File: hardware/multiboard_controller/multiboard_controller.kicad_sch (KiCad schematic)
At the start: 0 parts

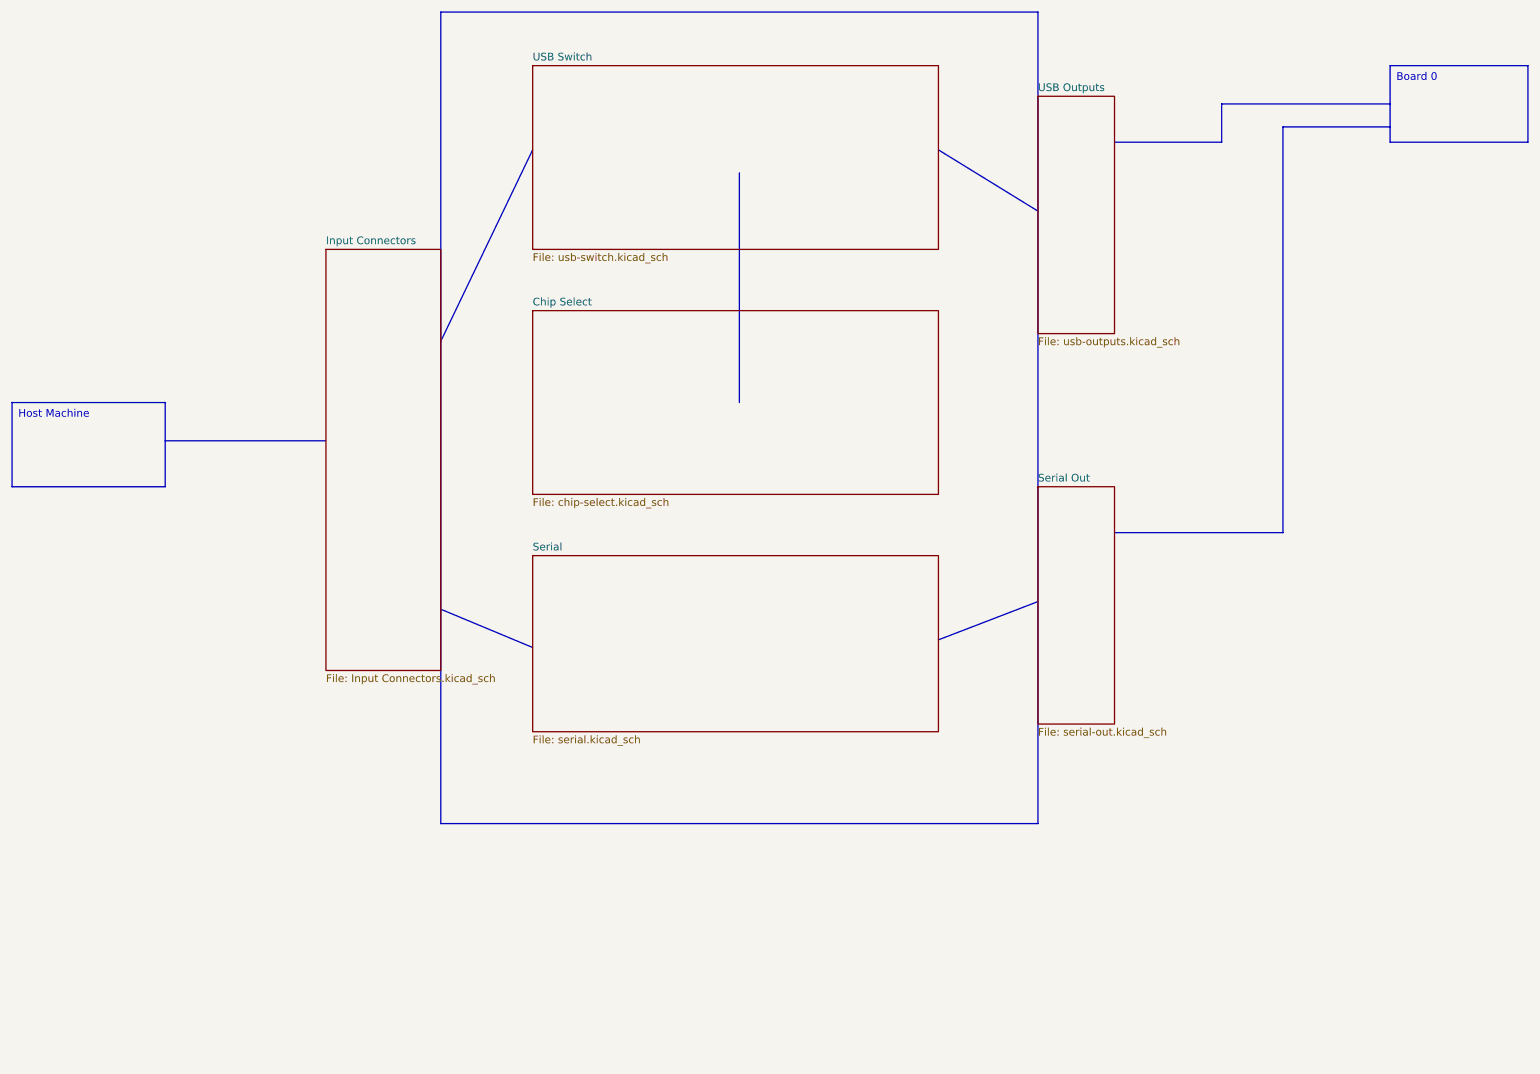
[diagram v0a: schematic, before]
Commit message: Add ESD protection for USB 2.0 ifaces.
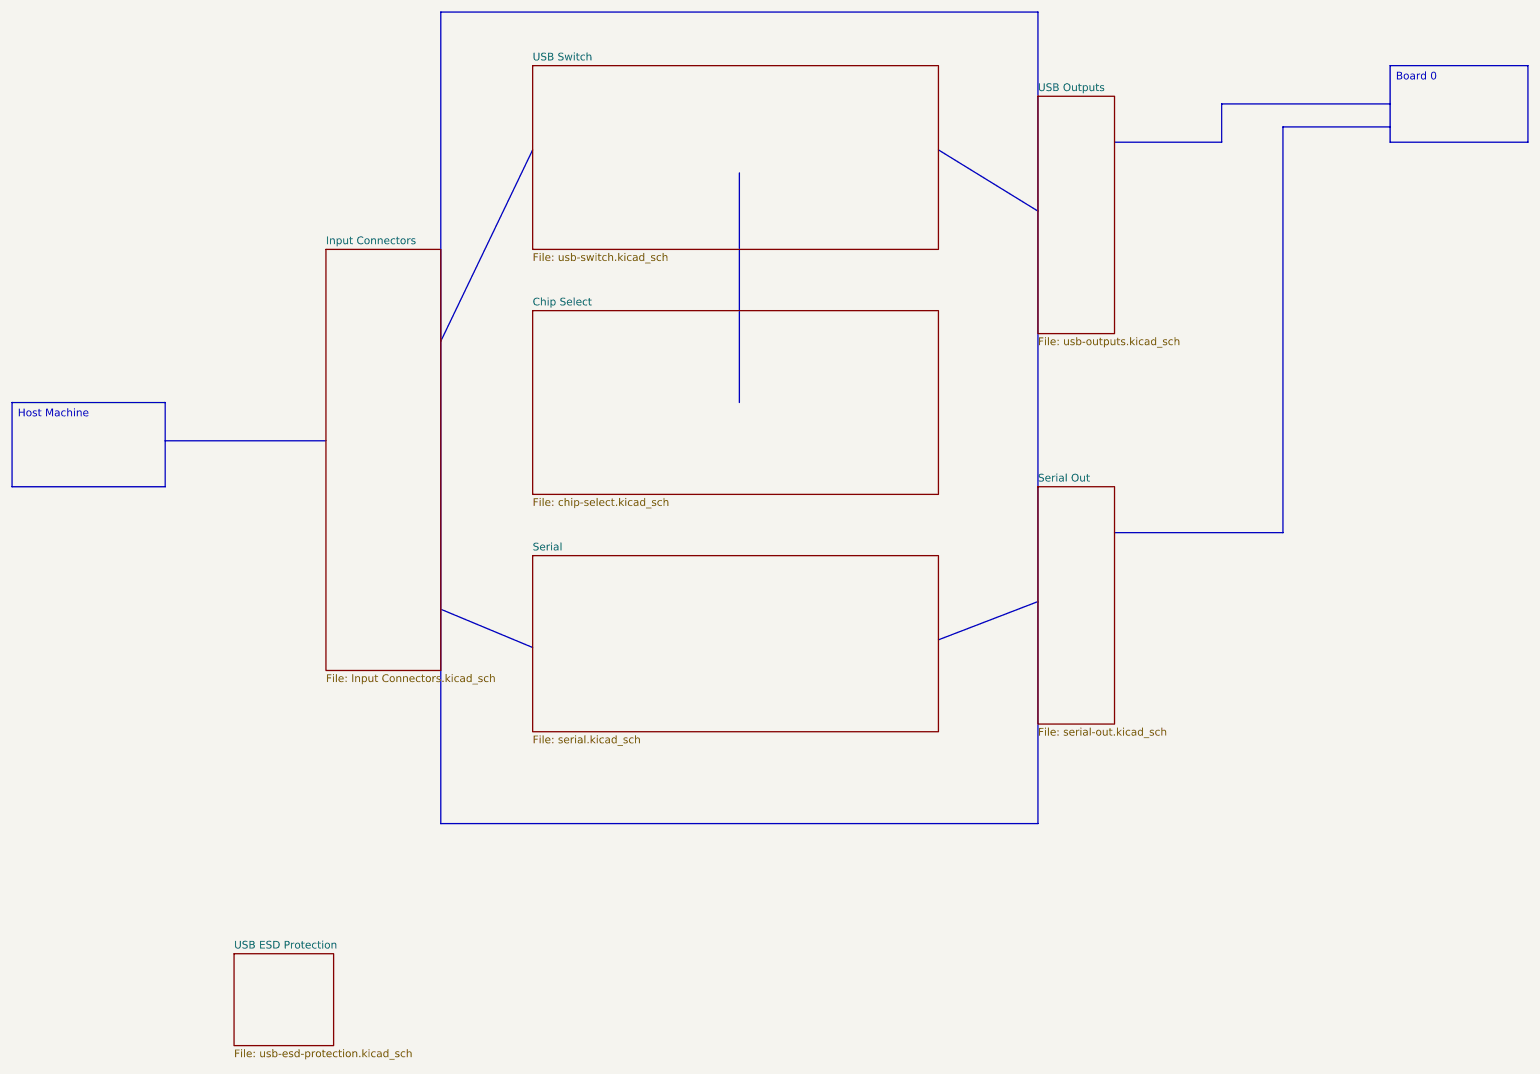
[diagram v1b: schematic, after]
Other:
- added sheet USB ESD Protection (usb-esd-protection.kicad_sch)
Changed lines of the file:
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@@
 (kicad_sch
-	(version 20231120)
+	(version 20250114)
 	(generator "eeschema")
-	(generator_version "8.0")
+	(generator_version "9.0")
 	(paper "A4")
 	(title_block
@@
 		(date "2025-02-12")
 	)
-	(polyline
-		(pts
-			(xy 90.17 72.39) (xy 105.41 40.64)
-		)
-		(stroke
-			(width 0)
-			(type default)
-		)
-	)
-	(polyline
-		(pts
-			(xy 90.17 116.84) (xy 105.41 123.19)
-		)
-		(stroke
-			(width 0)
-			(type default)
-		)
-	)
-	(polyline
-		(pts
-			(xy 219.71 39.37) (xy 219.71 33.02)
-		)
-		(stroke
-			(width 0)
-			(type default)
-		)
-	)
-	(polyline
-		(pts
-			(xy 44.45 88.9) (xy 71.12 88.9)
-		)
-		(stroke
-			(width 0)
-			(type default)
-		)
-	)
-	(polyline
-		(pts
-			(xy 172.72 121.92) (xy 189.23 115.57)
-		)
-		(stroke
-			(width 0)
-			(type default)
-		)
-	)
-	(polyline
-		(pts
-			(xy 229.87 36.83) (xy 247.65 36.83)
-		)
-		(stroke
-			(width 0)
-			(type default)
-		)
-	)
-	(polyline
-		(pts
-			(xy 172.72 40.64) (xy 189.23 50.8)
-		)
-		(stroke
-			(width 0)
-			(type default)
-		)
-	)
-	(polyline
-		(pts
-			(xy 229.87 104.14) (xy 229.87 36.83)
-		)
-		(stroke
-			(width 0)
-			(type default)
-		)
-	)
-	(polyline
-		(pts
-			(xy 139.7 44.45) (xy 139.7 82.55)
-		)
-		(stroke
-			(width 0)
-			(type default)
-		)
-	)
-	(polyline
-		(pts
-			(xy 201.93 104.14) (xy 229.87 104.14)
-		)
-		(stroke
-			(width 0)
-			(type default)
-		)
-	)
-	(polyline
-		(pts
-			(xy 219.71 33.02) (xy 247.65 33.02)
-		)
-		(stroke
-			(width 0)
-			(type default)
-		)
-	)
-	(polyline
-		(pts
-			(xy 201.93 39.37) (xy 219.71 39.37)
-		)
-		(stroke
-			(width 0)
-			(type default)
-		)
-	)
 	(rectangle
 		(start 90.17 17.78)
@@
 		(at 247.65 26.67 0)
 		(size 22.86 12.7)
+		(margins 0.9525 0.9525 0.9525 0.9525)
 		(stroke
 			(width 0)
@@
 		(at 19.05 82.55 0)
 		(size 25.4 13.97)
+		(margins 0.9525 0.9525 0.9525 0.9525)
 		(stroke
 			(width 0)
@@
 		)
 	)
+	(polyline
+		(pts
+			(xy 90.17 72.39) (xy 105.41 40.64)
+		)
+		(stroke
+			(width 0)
+			(type default)
+		)
+	)
+	(polyline
+		(pts
+			(xy 90.17 116.84) (xy 105.41 123.19)
+		)
+		(stroke
+			(width 0)
+			(type default)
+		)
+	)
+	(polyline
+		(pts
+			(xy 219.71 39.37) (xy 219.71 33.02)
+		)
+		(stroke
+			(width 0)
+			(type default)
+		)
+	)
+	(polyline
+		(pts
+			(xy 44.45 88.9) (xy 71.12 88.9)
+		)
+		(stroke
+			(width 0)
+			(type default)
+		)
+	)
+	(polyline
+		(pts
+			(xy 172.72 121.92) (xy 189.23 115.57)
+		)
+		(stroke
+			(width 0)
+			(type default)
+		)
+	)
+	(polyline
+		(pts
+			(xy 229.87 36.83) (xy 247.65 36.83)
+		)
+		(stroke
+			(width 0)
+			(type default)
+		)
+	)
+	(polyline
+		(pts
+			(xy 172.72 40.64) (xy 189.23 50.8)
+		)
+		(stroke
+			(width 0)
+			(type default)
+		)
+	)
+	(polyline
+		(pts
+			(xy 229.87 104.14) (xy 229.87 36.83)
+		)
+		(stroke
+			(width 0)
+			(type default)
+		)
+	)
+	(polyline
+		(pts
+			(xy 139.7 44.45) (xy 139.7 82.55)
+		)
+		(stroke
+			(width 0)
+			(type default)
+		)
+	)
+	(polyline
+		(pts
+			(xy 201.93 104.14) (xy 229.87 104.14)
+		)
+		(stroke
+			(width 0)
+			(type default)
+		)
+	)
+	(polyline
+		(pts
+			(xy 219.71 33.02) (xy 247.65 33.02)
+		)
+		(stroke
+			(width 0)
+			(type default)
+		)
+	)
+	(polyline
+		(pts
+			(xy 201.93 39.37) (xy 219.71 39.37)
+		)
+		(stroke
+			(width 0)
+			(type default)
+		)
+	)
 	(sheet
 		(at 71.12 57.15)
 		(size 19.05 69.85)
+		(exclude_from_sim no)
+		(in_bom yes)
+		(on_board yes)
+		(dnp no)
 		(fields_autoplaced yes)
 		(stroke
@@
 		(at 189.23 31.75)
 		(size 12.7 39.37)
+		(exclude_from_sim no)
+		(in_bom yes)
+		(on_board yes)
+		(dnp no)
 		(fields_autoplaced yes)
 		(stroke
@@
 		(at 105.41 26.67)
 		(size 67.31 30.48)
+		(exclude_from_sim no)
+		(in_bom yes)
+		(on_board yes)
+		(dnp no)
 		(fields_autoplaced yes)
 		(stroke
@@
 		(at 105.41 107.95)
 		(size 67.31 29.21)
+		(exclude_from_sim no)
+		(in_bom yes)
+		(on_board yes)
+		(dnp no)
 		(fields_autoplaced yes)
 		(stroke
@@
 		(at 105.41 67.31)
 		(size 67.31 30.48)
+		(exclude_from_sim no)
+		(in_bom yes)
+		(on_board yes)
+		(dnp no)
 		(fields_autoplaced yes)
 		(stroke
@@
 		(at 189.23 96.52)
 		(size 12.7 39.37)
+		(exclude_from_sim no)
+		(in_bom yes)
+		(on_board yes)
+		(dnp no)
 		(fields_autoplaced yes)
 		(stroke
@@
 				(path "/0fe19ce7-810a-40c6-903d-4212edc122f9"
 					(page "7")
+				)
+			)
+		)
+	)
+	(sheet
+		(at 55.88 173.99)
+		(size 16.51 15.24)
+		(exclude_from_sim no)
+		(in_bom yes)
+		(on_board yes)
+		(dnp no)
+		(fields_autoplaced yes)
+		(stroke
+			(width 0.1524)
+			(type solid)
+		)
+		(fill
+			(color 0 0 0 0.0000)
+		)
+		(property "Sheetname" "USB ESD Protection"
+			(at 55.88 173.2784 0)
+			(effects
+				(font
+					(size 1.27 1.27)
+				)
+				(justify left bottom)
+			)
+		)
+		(property "Sheetfile" "usb-esd-protection.kicad_sch"
+			(at 55.88 189.8146 0)
+			(effects
+				(font
+					(size 1.27 1.27)
+				)
+				(justify left top)
+			)
+		)
+		(instances
+			(project "multiboard_controller"
+				(path "/0fe19ce7-810a-40c6-903d-4212edc122f9"
+					(page "8")
 				)
 			)
@@
 		)
 	)
+	(embedded_fonts no)
 )
